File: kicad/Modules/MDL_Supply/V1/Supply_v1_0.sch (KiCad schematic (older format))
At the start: 28 parts, among them U1 LM555N

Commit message: update MDL and DB Supply
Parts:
- removed +12V1, +5V1: LM2940, symbol 78L05
- removed +3.3V1: LM1117T, symbol 78L05
- removed -12V1, -5V1: LM2990, symbol 78L05
- added U2: LM2940T-12.0/NOPB, symbol LM2940T-12.0/NOPB
- added U3: LM2940T-5.0/NOPB, symbol LM2940T-5.0/NOPB
- added U4: LM1117T-3.3/NOPB, symbol LM1117T-3.3/NOPB
- added U5: LM2990T-12.0/NOPB, symbol LM2990T-12.0/NOPB
- added U6: LM2990T-5.0/NOPB, symbol LM2990T-5.0/NOPB
- D2: renamed from 1N400X1; value D -> 1N4001
- D3: renamed from 1N400X2; value D -> 1N4001
- D4: renamed from 1N400X3; value D -> 1N4001
- Q1: renamed from 2N2222; value Q_NPN_BCE -> Q2N2222
- Q2: renamed from 2N2222_1; value Q_NPN_BCE -> Q2N2222
- Q3: renamed from 2N2907; value Q_PNP_BCE -> Q2N2907
- renumbered C6 to C10, C7 to C3, C8 to C4, C9 to C5, C10 to C6, C3 to C7, C4 to C8, C5 to C9, D5 to D1
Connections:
- wire segments 45 -> 47
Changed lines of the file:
@@
 LIBS:contrib
 LIBS:valves
+LIBS:echopen
 LIBS:Supply_v1_0-cache
 EELAYER 25 0
@@
 NoConn ~ 4750 3700
 $Comp
-L D 1N400X1
+L D D2
 U 1 1 572A15CB
 P 4900 5350
-F 0 "1N400X1" H 4900 5450 50  0000 C CNN
-F 1 "D" H 4900 5250 50  0000 C CNN
+F 0 "D2" H 4900 5450 50  0000 C CNN
+F 1 "1N4001" H 4900 5250 50  0000 C CNN
 F 2 "" H 4900 5350 50  0001 C CNN
 F 3 "" H 4900 5350 50  0000 C CNN
@@
 $EndComp
 $Comp
-L C C7
+L C C3
 U 1 1 572A164D
 P 5050 5650
-F 0 "C7" H 5075 5750 50  0000 L CNN
+F 0 "C3" H 5075 5750 50  0000 L CNN
 F 1 "220u" H 5075 5550 50  0000 L CNN
 F 2 "" H 5088 5500 50  0001 C CNN
@@
 $EndComp
 $Comp
-L C C8
+L C C4
 U 1 1 572A208B
 P 5850 5650
-F 0 "C8" H 5875 5750 50  0000 L CNN
+F 0 "C4" H 5875 5750 50  0000 L CNN
 F 1 "47u" H 5875 5550 50  0000 L CNN
 F 2 "" H 5888 5500 50  0001 C CNN
@@
 $EndComp
 $Comp
-L C C9
+L C C5
 U 1 1 572A239F
 P 6650 5650
-F 0 "C9" H 6675 5750 50  0000 L CNN
+F 0 "C5" H 6675 5750 50  0000 L CNN
 F 1 "47u" H 6675 5550 50  0000 L CNN
 F 2 "" H 6688 5500 50  0001 C CNN
@@
 $EndComp
 $Comp
-L LED D5
+L LED D1
 U 1 1 572A253C
 P 6950 5550
-F 0 "D5" H 6950 5650 50  0000 C CNN
+F 0 "D1" H 6950 5650 50  0000 C CNN
 F 1 "LED" H 6950 5450 50  0000 C CNN
 F 2 "" H 6950 5550 50  0001 C CNN
@@
 $EndComp
 $Comp
-L Q_NPN_BCE 2N2222
+L Q_NPN_BCE Q1
 U 1 1 572A387C
 P 5600 3700
-F 0 "2N2222" H 5900 3750 50  0000 R CNN
-F 1 "Q_NPN_BCE" H 6200 3650 50  0000 R CNN
+F 0 "Q1" H 5900 3750 50  0000 R CNN
+F 1 "Q2N2222" H 6200 3650 50  0000 R CNN
 F 2 "" H 5800 3800 50  0001 C CNN
 F 3 "" H 5600 3700 50  0000 C CNN
@@
 $EndComp
 $Comp
-L Q_NPN_BCE 2N2222_1
+L Q_NPN_BCE Q2
 U 1 1 572A3ACF
 P 6500 3400
-F 0 "2N2222_1" H 6800 3450 50  0000 R CNN
-F 1 "Q_NPN_BCE" H 7100 3350 50  0000 R CNN
+F 0 "Q2" H 6800 3450 50  0000 R CNN
+F 1 "Q2N2222" H 7100 3350 50  0000 R CNN
 F 2 "" H 6700 3500 50  0001 C CNN
 F 3 "" H 6500 3400 50  0000 C CNN
@@
 $EndComp
 $Comp
-L Q_PNP_BCE 2N2907
+L Q_PNP_BCE Q3
 U 1 1 572A3B5B
 P 6500 3800
-F 0 "2N2907" H 6800 3850 50  0000 R CNN
-F 1 "Q_PNP_BCE" H 7100 3750 50  0000 R CNN
+F 0 "Q3" H 6800 3850 50  0000 R CNN
+F 1 "Q2N2907" H 7100 3750 50  0000 R CNN
 F 2 "" H 6700 3900 50  0001 C CNN
 F 3 "" H 6500 3800 50  0000 C CNN
@@
 $EndComp
 $Comp
-L CP C3
+L CP C7
 U 1 1 572A3DB6
 P 7350 3600
-F 0 "C3" H 7375 3700 50  0000 L CNN
+F 0 "C7" H 7375 3700 50  0000 L CNN
 F 1 "47u" H 7375 3500 50  0000 L CNN
 F 2 "" H 7388 3450 50  0001 C CNN
@@
 $EndComp
 $Comp
-L D 1N400X2
+L D D3
 U 1 1 572A3EDF
 P 7500 3750
-F 0 "1N400X2" H 7500 3850 50  0000 C CNN
-F 1 "D" H 7500 3650 50  0000 C CNN
+F 0 "D3" H 7500 3850 50  0000 C CNN
+F 1 "1N4001" H 7500 3650 50  0000 C CNN
 F 2 "" H 7500 3750 50  0001 C CNN
 F 3 "" H 7500 3750 50  0000 C CNN
@@
 $EndComp
 $Comp
-L D 1N400X3
+L D D4
 U 1 1 572A4183
 P 7650 3600
-F 0 "1N400X3" H 7650 3700 50  0000 C CNN
-F 1 "D" H 7650 3500 50  0000 C CNN
+F 0 "D4" H 7650 3700 50  0000 C CNN
+F 1 "1N4001" H 7650 3500 50  0000 C CNN
 F 2 "" H 7650 3600 50  0001 C CNN
 F 3 "" H 7650 3600 50  0000 C CNN
@@
 $EndComp
 $Comp
-L CP C4
+L CP C8
 U 1 1 572A41F8
 P 7800 3750
-F 0 "C4" H 7825 3850 50  0000 L CNN
+F 0 "C8" H 7825 3850 50  0000 L CNN
 F 1 "47u" H 7825 3650 50  0000 L CNN
 F 2 "" H 7838 3600 50  0001 C CNN
@@
 $EndComp
 $Comp
-L CP C5
+L CP C9
 U 1 1 572A43A2
 P 8600 3750
-F 0 "C5" H 8625 3850 50  0000 L CNN
+F 0 "C9" H 8625 3850 50  0000 L CNN
 F 1 "47u" H 8625 3650 50  0000 L CNN
 F 2 "" H 8638 3600 50  0001 C CNN
@@
 NoConn ~ 5050 3700
 $Comp
-L 78L05 -12V1
-U 1 1 575A0CF3
-P 8200 3650
-F 0 "-12V1" H 8350 3454 50  0000 C CNN
-F 1 "LM2990" H 8200 3850 50  0000 C CNN
-F 2 "" H 8200 3650 50  0001 C CNN
-F 3 "" H 8200 3650 50  0000 C CNN
-	1    8200 3650
-	1    0    0    -1
-$EndComp
-$Comp
-L 78L05 -5V1
-U 1 1 575A10F8
-P 9000 3650
-F 0 "-5V1" H 9150 3454 50  0000 C CNN
-F 1 "LM2990" H 9000 3850 50  0000 C CNN
-F 2 "" H 9000 3650 50  0001 C CNN
-F 3 "" H 9000 3650 50  0000 C CNN
-	1    9000 3650
-	1    0    0    -1
-$EndComp
-$Comp
-L CP C6
+L CP C10
 U 1 1 575A1244
 P 9400 3750
-F 0 "C6" H 9425 3850 50  0000 L CNN
+F 0 "C10" H 9425 3850 50  0000 L CNN
 F 1 "47u" H 9425 3650 50  0000 L CNN
 F 2 "" H 9438 3600 50  0001 C CNN
@@
 	1    0    0    1
 $EndComp
-$Comp
-L 78L05 +12V1
-U 1 1 575A672C
-P 5450 5400
-F 0 "+12V1" H 5600 5204 50  0000 C CNN
-F 1 "LM2940" H 5450 5600 50  0000 C CNN
-F 2 "" H 5450 5400 50  0001 C CNN
-F 3 "" H 5450 5400 50  0000 C CNN
-	1    5450 5400
-	1    0    0    -1
-$EndComp
-$Comp
-L 78L05 +5V1
-U 1 1 575A9393
-P 6250 5400
-F 0 "+5V1" H 6400 5204 50  0000 C CNN
-F 1 "LM2940" H 6250 5600 50  0000 C CNN
-F 2 "" H 6250 5400 50  0001 C CNN
-F 3 "" H 6250 5400 50  0000 C CNN
-	1    6250 5400
-	1    0    0    -1
-$EndComp
 NoConn ~ 3350 4350
 Text Label 8150 7650 0    60   ~ 0
@@
 Alimentation_Symétrique_+/-_5V;12V
 $Comp
-L 78L05 +3.3V1
-U 1 1 57A2E6B8
-P 6300 4400
-F 0 "+3.3V1" H 6450 4204 50  0000 C CNN
-F 1 "LM1117T" H 6300 4600 50  0000 C CNN
-F 2 "" H 6300 4400 50  0001 C CNN
-F 3 "" H 6300 4400 50  0000 C CNN
-	1    6300 4400
-	1    0    0    -1
-$EndComp
-$Comp
-L CP C10
+L CP C6
 U 1 1 57A2E7D0
 P 6700 4500
-F 0 "C10" H 6725 4600 50  0000 L CNN
+F 0 "C6" H 6725 4600 50  0000 L CNN
 F 1 "47u" H 6725 4400 50  0000 L CNN
 F 2 "" H 6738 4350 50  0001 C CNN
@@
 Text GLabel 7050 4350 2    60   Input ~ 0
 3.3V
-Text GLabel 8600 3600 1    60   Input ~ 0
+Text GLabel 8600 3250 1    60   Input ~ 0
 -12V
-Text GLabel 9400 3600 1    60   Input ~ 0
+Text GLabel 9400 3250 1    60   Input ~ 0
 -5V
+$Comp
+L LM2940T-12.0/NOPB U2
+U 1 1 57AB3A8D
+P 5450 5400
+F 0 "U2" H 5600 5204 50  0000 C CNN
+F 1 "LM2940T-12.0/NOPB" H 5450 5600 50  0000 C CNN
+F 2 "" H 5450 5400 50  0000 C CNN
+F 3 "" H 5450 5400 50  0000 C CNN
+	1    5450 5400
+	1    0    0    -1
+$EndComp
+$Comp
+L LM2940T-5.0/NOPB U3
+U 1 1 57AB3B35
+P 6250 5400
+F 0 "U3" H 6400 5204 50  0000 C CNN
+F 1 "LM2940T-5.0/NOPB" H 6250 5600 50  0000 C CNN
+F 2 "" H 6250 5400 50  0000 C CNN
+F 3 "" H 6250 5400 50  0000 C CNN
+	1    6250 5400
+	1    0    0    -1
+$EndComp
+$Comp
+L LM1117T-3.3/NOPB U4
+U 1 1 57AB3BF3
+P 6300 4400
+F 0 "U4" H 6450 4204 50  0000 C CNN
+F 1 "LM1117T-3.3/NOPB" H 6300 4600 50  0000 C CNN
+F 2 "" H 6300 4400 50  0000 C CNN
+F 3 "" H 6300 4400 50  0000 C CNN
+	1    6300 4400
+	1    0    0    -1
+$EndComp
+$Comp
+L LM2990T-12.0/NOPB U5
+U 1 1 57AB439B
+P 8200 3650
+F 0 "U5" H 8350 3454 50  0000 C CNN
+F 1 "LM2990T-12.0/NOPB" H 8200 3850 50  0000 C CNN
+F 2 "" H 8200 3650 50  0000 C CNN
+F 3 "" H 8200 3650 50  0000 C CNN
+	1    8200 3650
+	1    0    0    -1
+$EndComp
+$Comp
+L LM2990T-5.0/NOPB U6
+U 1 1 57AB44AB
+P 9000 3650
+F 0 "U6" H 9150 3454 50  0000 C CNN
+F 1 "LM2990T-5.0/NOPB" H 9000 3850 50  0000 C CNN
+F 2 "" H 9000 3650 50  0000 C CNN
+F 3 "" H 9000 3650 50  0000 C CNN
+	1    9000 3650
+	1    0    0    -1
+$EndComp
+Wire Wire Line
+	8600 3600 8600 3250
+Wire Wire Line
+	9400 3600 9400 3250
 $EndSCHEMATC

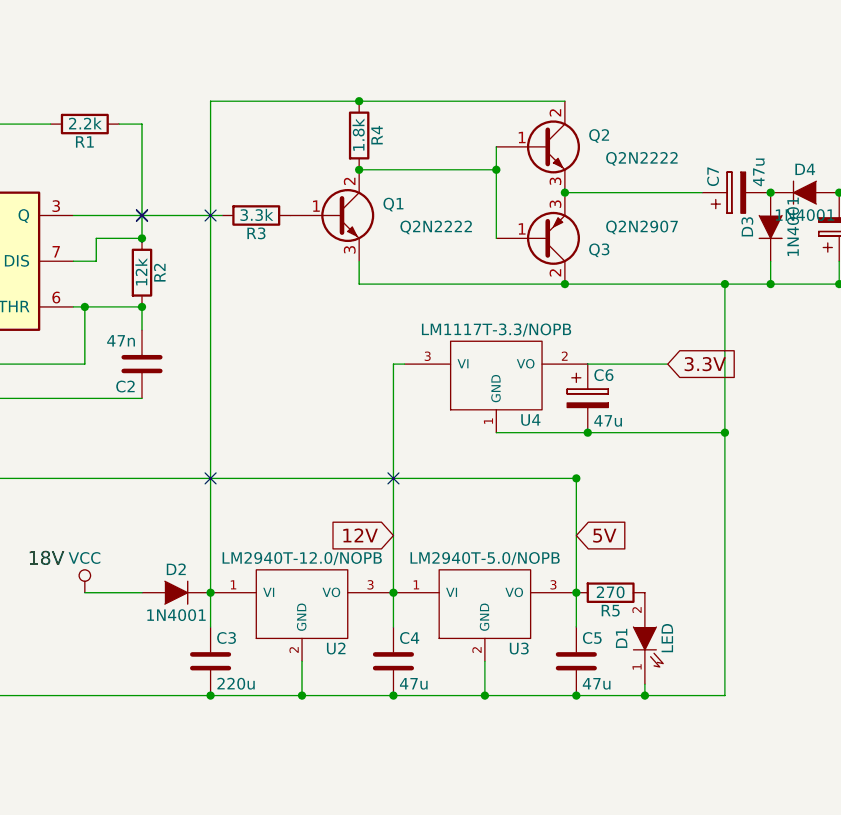
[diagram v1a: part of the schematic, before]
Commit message: update DB_HV, update librairy and librairy path for MDL
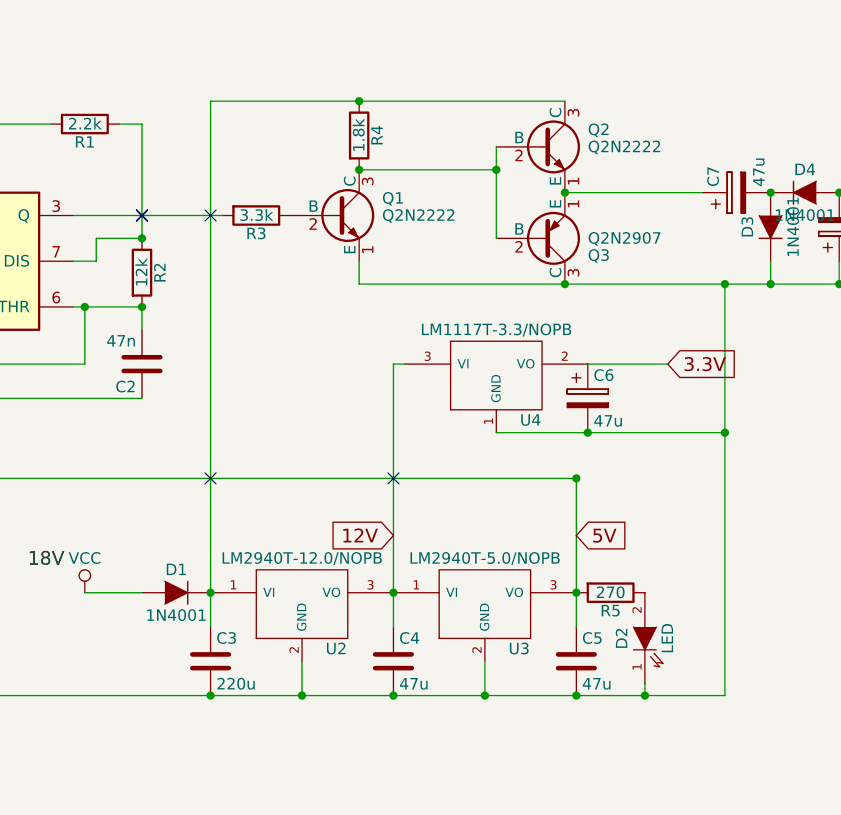
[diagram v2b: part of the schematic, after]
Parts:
- removed Q1, Q2: Q2N2222, symbol Q_NPN_BCE
- removed Q3: Q2N2907, symbol Q_PNP_BCE
- added Q1, Q2: Q2N2222, symbol Q2N2222
- added Q3: Q2N2907, symbol Q2N2907
- renumbered D2 to D1, D1 to D2
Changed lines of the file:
@@
 NoConn ~ 4750 3700
 $Comp
-L D D2
+L D D1
 U 1 1 572A15CB
 P 4900 5350
-F 0 "D2" H 4900 5450 50  0000 C CNN
+F 0 "D1" H 4900 5450 50  0000 C CNN
 F 1 "1N4001" H 4900 5250 50  0000 C CNN
 F 2 "" H 4900 5350 50  0001 C CNN
@@
 $EndComp
 $Comp
-L LED D1
+L LED D2
 U 1 1 572A253C
 P 6950 5550
-F 0 "D1" H 6950 5650 50  0000 C CNN
+F 0 "D2" H 6950 5650 50  0000 C CNN
 F 1 "LED" H 6950 5450 50  0000 C CNN
 F 2 "" H 6950 5550 50  0001 C CNN
@@
 	1    6950 5550
 	0    -1   -1   0
-$EndComp
-$Comp
-L Q_NPN_BCE Q1
-U 1 1 572A387C
-P 5600 3700
-F 0 "Q1" H 5900 3750 50  0000 R CNN
-F 1 "Q2N2222" H 6200 3650 50  0000 R CNN
-F 2 "" H 5800 3800 50  0001 C CNN
-F 3 "" H 5600 3700 50  0000 C CNN
-	1    5600 3700
-	1    0    0    -1
 $EndComp
 $Comp
@@
 	1    5700 3350
 	1    0    0    -1
-$EndComp
-$Comp
-L Q_NPN_BCE Q2
-U 1 1 572A3ACF
-P 6500 3400
-F 0 "Q2" H 6800 3450 50  0000 R CNN
-F 1 "Q2N2222" H 7100 3350 50  0000 R CNN
-F 2 "" H 6700 3500 50  0001 C CNN
-F 3 "" H 6500 3400 50  0000 C CNN
-	1    6500 3400
-	1    0    0    -1
-$EndComp
-$Comp
-L Q_PNP_BCE Q3
-U 1 1 572A3B5B
-P 6500 3800
-F 0 "Q3" H 6800 3850 50  0000 R CNN
-F 1 "Q2N2907" H 7100 3750 50  0000 R CNN
-F 2 "" H 6700 3900 50  0001 C CNN
-F 3 "" H 6500 3800 50  0000 C CNN
-	1    6500 3800
-	1    0    0    1
 $EndComp
 $Comp
@@
 Wire Wire Line
 	9400 3600 9400 3250
+$Comp
+L Q2N2222 Q1
+U 1 1 57B43190
+P 5600 3700
+F 0 "Q1" H 5800 3775 50  0000 L CNN
+F 1 "Q2N2222" H 5800 3700 50  0000 L CNN
+F 2 "" H 5800 3625 50  0000 L CIN
+F 3 "" H 5600 3700 50  0000 L CNN
+	1    5600 3700
+	1    0    0    -1
+$EndComp
+$Comp
+L Q2N2222 Q2
+U 1 1 57B431FB
+P 6500 3400
+F 0 "Q2" H 6700 3475 50  0000 L CNN
+F 1 "Q2N2222" H 6700 3400 50  0000 L CNN
+F 2 "" H 6700 3325 50  0000 L CIN
+F 3 "" H 6500 3400 50  0000 L CNN
+	1    6500 3400
+	1    0    0    -1
+$EndComp
+$Comp
+L Q2N2907 Q3
+U 1 1 57B4327C
+P 6500 3800
+F 0 "Q3" H 6700 3875 50  0000 L CNN
+F 1 "Q2N2907" H 6700 3800 50  0000 L CNN
+F 2 "" H 6800 3650 50  0000 L CIN
+F 3 "" H 6500 3800 50  0000 L CNN
+	1    6500 3800
+	1    0    0    1
+$EndComp
 $EndSCHEMATC

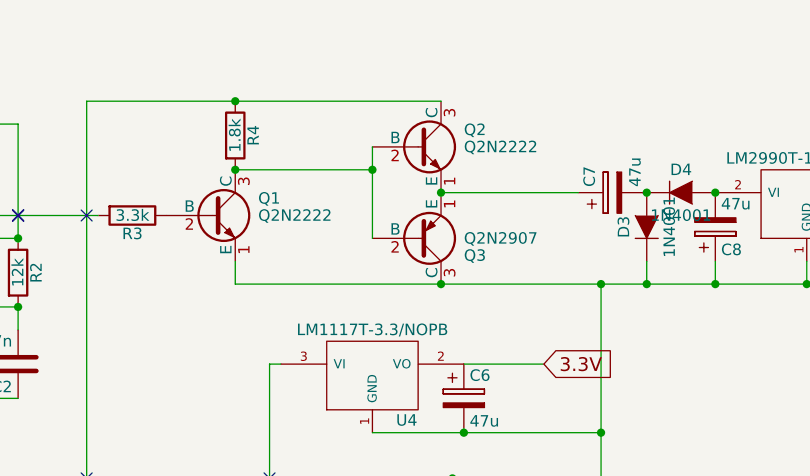
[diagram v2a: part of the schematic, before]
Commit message: update MDLs with new librairy
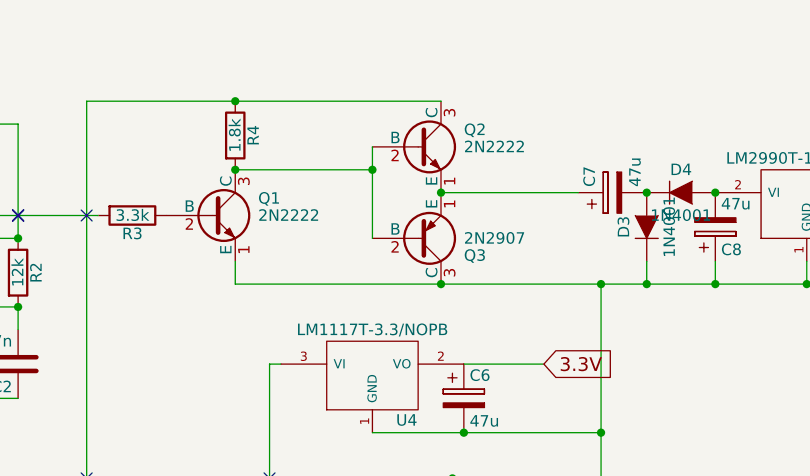
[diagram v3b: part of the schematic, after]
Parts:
- removed Q1, Q2: Q2N2222, symbol Q2N2222
- removed Q3: Q2N2907, symbol Q2N2907
- added Q1, Q2: 2N2222, symbol 2N2222
- added Q3: 2N2907, symbol 2N2907
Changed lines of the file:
@@
 	9400 3600 9400 3250
 $Comp
-L Q2N2222 Q1
-U 1 1 57B43190
+L 2N2222 Q1
+U 1 1 57B474C6
 P 5600 3700
 F 0 "Q1" H 5800 3775 50  0000 L CNN
-F 1 "Q2N2222" H 5800 3700 50  0000 L CNN
+F 1 "2N2222" H 5800 3700 50  0000 L CNN
 F 2 "" H 5800 3625 50  0000 L CIN
 F 3 "" H 5600 3700 50  0000 L CNN
@@
 $EndComp
 $Comp
-L Q2N2222 Q2
-U 1 1 57B431FB
+L 2N2222 Q2
+U 1 1 57B4754C
 P 6500 3400
 F 0 "Q2" H 6700 3475 50  0000 L CNN
-F 1 "Q2N2222" H 6700 3400 50  0000 L CNN
+F 1 "2N2222" H 6700 3400 50  0000 L CNN
 F 2 "" H 6700 3325 50  0000 L CIN
 F 3 "" H 6500 3400 50  0000 L CNN
@@
 $EndComp
 $Comp
-L Q2N2907 Q3
-U 1 1 57B4327C
+L 2N2907 Q3
+U 1 1 57B475F0
 P 6500 3800
 F 0 "Q3" H 6700 3875 50  0000 L CNN
-F 1 "Q2N2907" H 6700 3800 50  0000 L CNN
+F 1 "2N2907" H 6700 3800 50  0000 L CNN
 F 2 "" H 6800 3650 50  0000 L CIN
 F 3 "" H 6500 3800 50  0000 L CNN
